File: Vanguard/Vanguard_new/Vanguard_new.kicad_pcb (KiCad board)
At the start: 4 copper layers, 683.3 x 251 mm, 70 parts, among them J1 USB_C, J2 Conn_02x03_Pin, J3 Micro_SD_Card_Det1, J4 STARBOARD_SERVO, J5 PORTSIDE_SERVO, Q1 BSS138, Q2 BSS138, Q3 BSS138, Q4 BSS138, U1 ATSAMD11D14A-M, U2 ATmega4809-A, U3 AT25DF641A-SH-T, U4 AP2112K-3.3, U5 MPM3610AGQV-P, U6 BNO086, U7 TXB0104D, U8 TPS61092, Y1 32.768kHz

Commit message: usb input almost done
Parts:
- added J6: LIPO_in, Wago-2601-1102:CONN2_2601-1102_WAG, F.Cu at (240.0, 114.5)
- J2: footprint Connector_PinHeader_2.54mm:PinHeader_1x03_P2.54mm_Vertical -> Connector_PinHeader_2.54mm:PinHeader_2x03_P2.54mm_Vertical
- moved Q3 311.1 mm to (354.8, 15.3), turned to -90 degrees
- moved Q2 310.5 mm to (352.8, 19.3)
- moved Q1 310.5 mm to (356.3, 19.3)
- moved U1 304.3 mm to (348.0, 16.3), turned to -45 degrees
- moved J1 303.2 mm to (336.8, 24.6), turned to 90 degrees
- moved J2 294.8 mm to (346.3, 27.9)
- moved D2 244.8 mm to (356.8, 25.4), turned to 0 degrees
- moved D3 244.7 mm to (355.0, 25.4), turned to 0 degrees
- moved TP1 236.5 mm to (342.3, 17.9), turned to 90 degrees
- moved D1 226.3 mm to (340.8, 24.4), turned to 180 degrees
- moved R7 225.3 mm to (357.3, 13.9), turned to 90 degrees
- moved TP2 223.8 mm to (338.3, 17.9), turned to 90 degrees
- moved R6 222.1 mm to (357.3, 22.4), turned to 90 degrees
- moved R12 221.5 mm to (357.3, 15.9)
- moved R5 221.1 mm to (358.3, 22.4)
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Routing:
- net RST: track 38.9 -> 84.4 mm, vias 0 -> 3
- net VBUS_out: track 15.0 -> 50.3 mm, vias 0 -> 4
- net UPDI: track 0.00 -> 28.0 mm, vias 0 -> 2
- net Net-(D1-I/O2): track 0.00 -> 26.5 mm, vias 0 -> 2
- net Net-(D1-I/O1): track 0.00 -> 20.3 mm, vias 0 -> 2
- net Net-(J2-Pin_2): track 0.00 -> 19.2 mm, vias 0 -> 2
- net Net-(D2-K): track 0.00 -> 17.9 mm, vias 0 -> 2
- net Net-(J2-Pin_6): track 0.00 -> 17.7 mm, vias 0 -> 2
- net /RX_UPDI: track 0.00 -> 17.6 mm
- net Net-(D3-K): track 0.00 -> 11.0 mm, vias 0 -> 2
- net GND: track 31.0 -> 37.9 mm
- net TX0: track 0.00 -> 6.48 mm, vias 0 -> 2
- net RX0: track 0.00 -> 2.51 mm
- net Net-(D2-A): track 0.00 -> 1.33 mm
- net Net-(D3-A): track 0.00 -> 1.00 mm

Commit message: pcb laying out
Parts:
- J6: value LIPO_in -> Conn_01x02_Pin; footprint Wago-2601-1102:CONN2_2601-1102_WAG -> Connector_PinHeader_2.54mm:PinHeader_1x02_P2.54mm_Vertical
- TP1, TP2: footprint TestPoint:TestPoint_2Pads_Pitch5.08mm_Drill1.3mm -> TestPoint:TestPoint_Pad_1.0x1.0mm
- moved U7 353.9 mm to (355.0, -11.9), turned to 0 degrees
- moved J3 332.3 mm to (343.1, -10.5), turned to 90 degrees
- moved U3 282.3 mm to (364.5, 18.0), turned to 180 degrees
- moved U2 224.7 mm to (357.7, 4.94), turned to 135 degrees
- moved R2 203.2 mm to (346.5, 25.0), turned to 90 degrees
- moved J6 169.3 mm to (378.5, 17.1)
- moved C10 157.8 mm to (374.1, 13.9), turned to 180 degrees
- moved C9 156.6 mm to (374.1, 14.7), turned to 180 degrees
- moved L1 154.0 mm to (370.9, 15.0), turned to 0 degrees
- moved U8 149.8 mm to (373.6, 18.4), turned to -90 degrees
- moved C8 146.5 mm to (369.8, 18.9), turned to 90 degrees
- moved TP2 1.70 mm to (340.0, 17.9)
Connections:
- J6 pad 1: GND -> VBUS_out
- J6 pad 2: unconnected-(J6-1_2-Pad2) -> GND
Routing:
- net RST: track 84.4 -> 123.4 mm, vias 3 -> 5
- net VBUS_out: track 50.3 -> 74.6 mm
- net PA3/SS: track 0.00 -> 19.2 mm, vias 0 -> 2
- net PA0/MISO: track 0.00 -> 18.5 mm, vias 0 -> 2
- net Net-(J2-Pin_3): track 0.00 -> 17.5 mm, vias 0 -> 2
- net D7: track 0.00 -> 16.1 mm, vias 0 -> 2
- net PA2/SCK: track 0.00 -> 15.8 mm, vias 0 -> 2
- net D4: track 0.00 -> 15.4 mm, vias 0 -> 2
- net D6: track 0.00 -> 15.0 mm
- net CD: track 0.00 -> 14.8 mm, vias 0 -> 2
- net D5: track 0.00 -> 14.1 mm, vias 0 -> 2
- net GND: track 37.9 -> 49.2 mm, vias 13 -> 15
- net PA1/MOSI: track 0.00 -> 10.9 mm
- net Net-(D1-I/O1): track 20.3 -> 30.1 mm
- net BUZZER: track 0.00 -> 9.17 mm
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
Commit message: finished pcb wiring
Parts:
- moved R21 296.2 mm to (359.5, 13.5)
- moved C2 294.3 mm to (337.0, 12.5), turned to 90 degrees
- moved ADR1 294.0 mm to (341.8, 8.06)
- moved C3 294.0 mm to (337.0, 14.2), turned to -90 degrees
- moved R18 293.9 mm to (346.4, 12.5)
- moved R19 293.9 mm to (346.4, 10.2)
- moved C7 293.9 mm to (346.0, 13.0)
- moved R20 293.9 mm to (344.8, 8.64)
- moved R23 293.9 mm to (344.6, 7.49)
- moved U6 293.9 mm to (343.1, 12.2)
- moved Y1 293.9 mm to (339.2, 12.3)
- moved R24 293.6 mm to (343.0, 16.0), turned to 0 degrees
- moved R22 292.8 mm to (361.5, 10.5), turned to 135 degrees
- moved R9 215.5 mm to (356.5, 12.0), turned to 180 degrees
- moved R10 213.4 mm to (354.2, 23.9), turned to 90 degrees
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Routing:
- net +5V: track 2.97 -> 78.5 mm, vias 0 -> 2
- net RST: track 123.4 -> 175.3 mm, vias 5 -> 12
- net GND: track 49.2 -> 81.2 mm, vias 15 -> 28
- net STAR_SERVO: track 0.00 -> 27.3 mm, vias 0 -> 1
- net PORT_SERVO: track 0.00 -> 27.2 mm, vias 0 -> 1
- net SCL: track 0.00 -> 25.2 mm, vias 0 -> 2
- net SDA: track 0.00 -> 23.8 mm, vias 0 -> 4
- net TX0: track 6.48 -> 19.0 mm, vias 2 -> 4
- net RX0: track 2.51 -> 14.5 mm, vias 0 -> 2
- net STAR_RED: track 0.00 -> 8.11 mm, vias 0 -> 2
- net UPDI: track 27.8 -> 35.4 mm, vias 2 -> 4
- net VBUS_out: track 74.6 -> 82.2 mm, vias 4 -> 6
- net PORT_RED: track 0.00 -> 7.05 mm
- net STAR_GREEN: track 0.00 -> 6.01 mm
- net PORT_GREEN: track 0.00 -> 5.59 mm, vias 0 -> 2
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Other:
- board size 683.3 x 251 mm -> 45 x 52.5 mm

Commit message: few silkscreen
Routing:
- net RST: track 175.3 -> 174.5 mm
- net Net-(J2-Pin_6): track 17.8 -> 18.4 mm

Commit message: small changes
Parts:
- moved Q4 257.4 mm to (134.0, 105.1)
- moved BZ1 256.0 mm to (144.6, 100.7)
- moved R11 252.6 mm to (121.0, 125.6), turned to 180 degrees
- moved C7 252.4 mm to (117.1, 119.4)
- moved C8 252.3 mm to (140.9, 124.9)
- moved STARBOARD_RGB1 252.3 mm to (141.0, 109.5)
- moved ADR1 252.3 mm to (112.9, 114.0)
- moved C1 252.3 mm to (115.5, 130.1)
- moved C10 252.3 mm to (145.1, 119.9)
- moved C4 252.3 mm to (132.5, 130.5)
- moved C5 252.3 mm to (142.5, 131.2)
- moved C6 252.3 mm to (146.2, 129.0)
- moved C9 252.3 mm to (145.1, 120.6)
- moved D1 252.3 mm to (111.8, 130.3)
- moved D2 252.3 mm to (127.8, 131.3)
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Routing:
- net +5V: track 78.5 -> 66.4 mm
- net BUZZER: track 9.17 -> 3.84 mm
- net Net-(U6-XIN32): track 5.51 -> 4.12 mm
- net Net-(BZ1--): track 7.23 -> 6.07 mm
- net Net-(U6-XOUT32/CLKSEL1): track 5.28 -> 4.19 mm
- net Net-(J2-Pin_6): track 18.4 -> 18.9 mm
- net GND: track 81.2 -> 80.8 mm, vias 28 -> 29
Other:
- board size 45 x 52.5 mm -> 46.2 x 50.9 mm

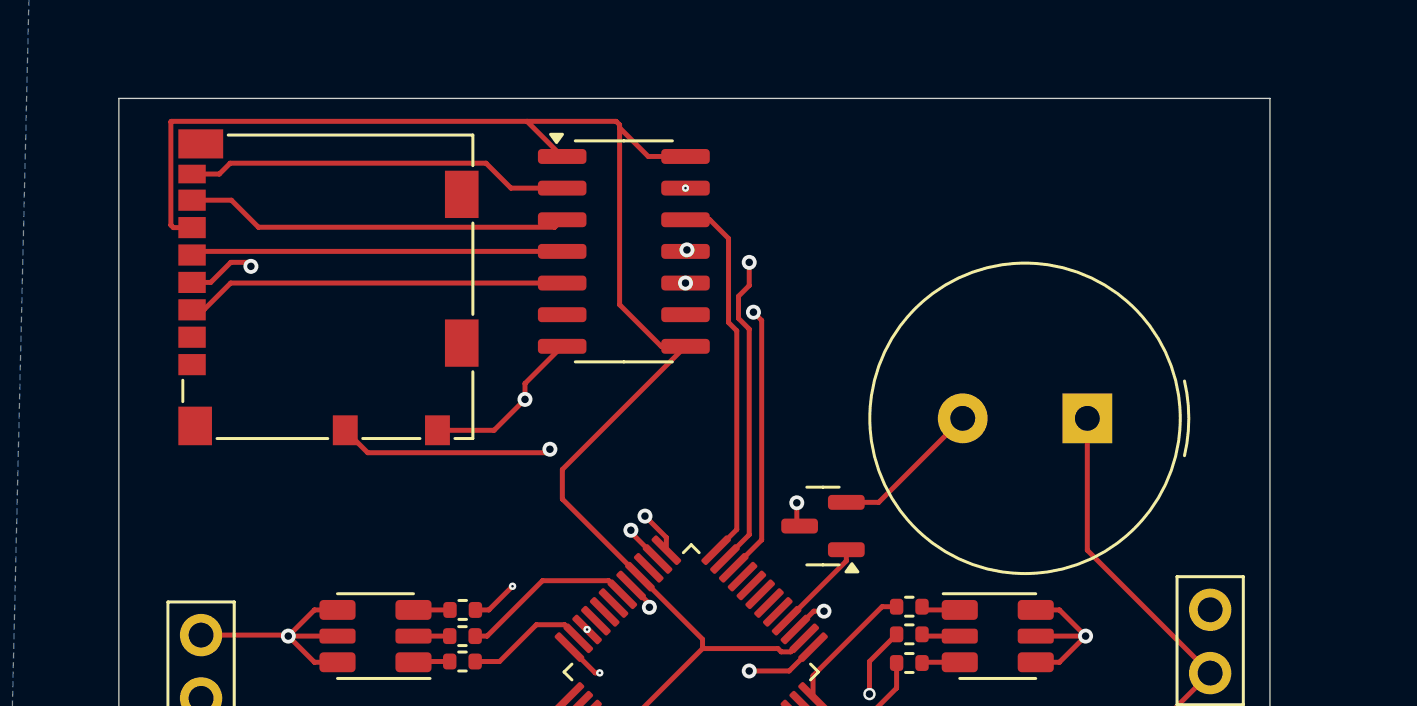
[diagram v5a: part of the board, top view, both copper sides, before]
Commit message: add 2 labels
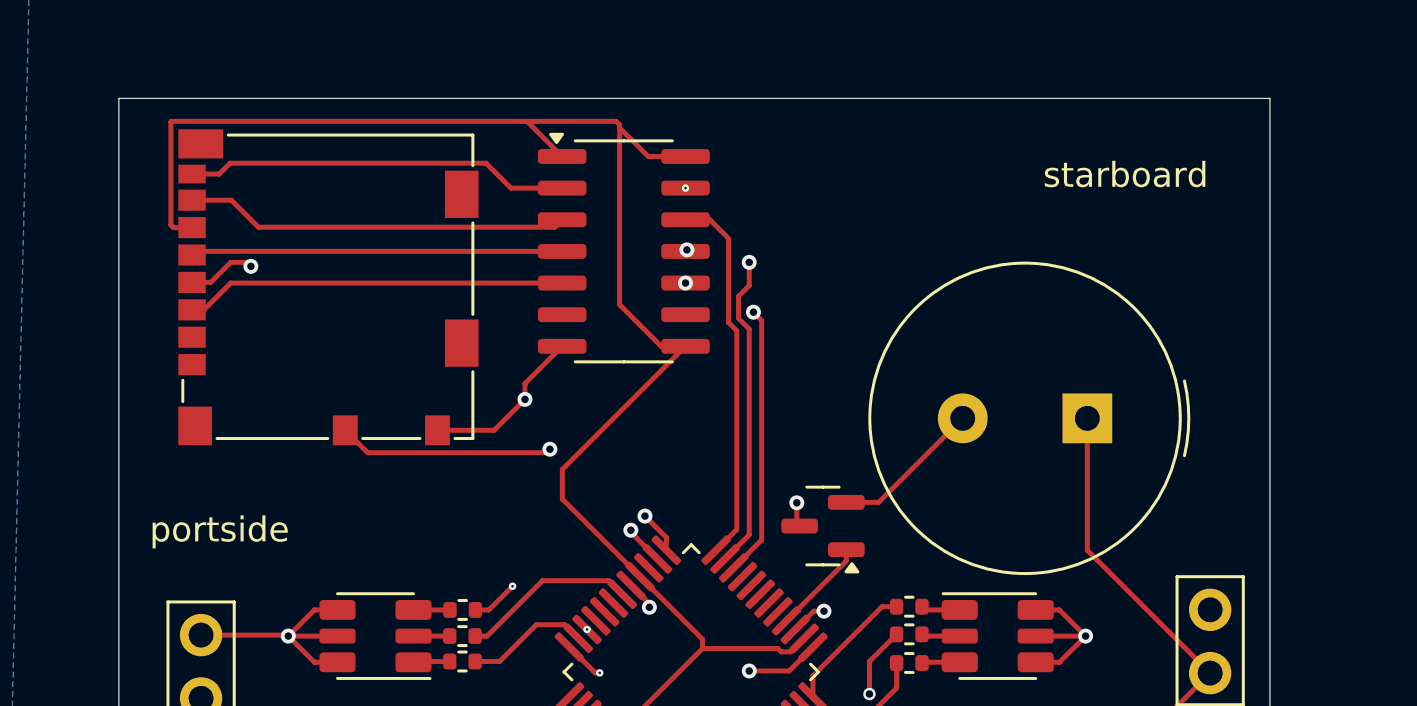
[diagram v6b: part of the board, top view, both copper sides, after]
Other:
- board text added: "portside"
- board text added: "starboard"
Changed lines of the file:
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@@
 		(tags "resistor")
 		(property "Reference" "R11"
-			(at 0 -1.17 360)
+			(at 0 -1.17 0)
 			(layer "F.SilkS")
 			(hide yes)
@@
 		)
 		(property "Value" "4k7"
-			(at 0 1.17 360)
+			(at 0 1.17 0)
 			(layer "F.Fab")
 			(effects
@@
 		)
 		(fp_text user "${REFERENCE}"
-			(at 0 0 360)
+			(at 0 0 0)
 			(layer "F.Fab")
 			(effects
@@
 		(tags "capacitor")
 		(property "Reference" "C2"
-			(at 28.55 -0.18 360)
+			(at 28.55 -0.18 0)
 			(layer "F.SilkS")
 			(hide yes)
@@
 		)
 		(property "Value" "22pF"
-			(at 28.550001 1.92 360)
+			(at 28.550001 1.92 0)
 			(layer "F.Fab")
 			(effects
@@
 		)
 		(fp_text user "${REFERENCE}"
-			(at 0 -0.680001 360)
+			(at 0 -0.680001 0)
 			(layer "F.Fab")
 			(effects
@@
 		(tags "capacitor")
 		(property "Reference" "C3"
-			(at 28.55 -0.18 360)
+			(at 28.55 -0.18 0)
 			(layer "F.SilkS")
 			(hide yes)
@@
 		)
 		(property "Value" "22pF"
-			(at 28.550001 1.92 360)
+			(at 28.550001 1.92 0)
 			(layer "F.Fab")
 			(effects
@@
 		)
 		(fp_text user "${REFERENCE}"
-			(at 0 -0.680001 360)
+			(at 0 -0.680001 0)
 			(layer "F.Fab")
 			(effects
@@
 		(layer "Edge.Cuts")
 	)
+	(gr_text "starboard"
+		(at 142.83 91.57 0)
+		(layer "F.SilkS")
+		(effects
+			(font
+				(size 1 1)
+				(thickness 0.1)
+			)
+			(justify left bottom)
+		)
+	)
+	(gr_text "portside"
+		(at 106.97 105.8 0)
+		(layer "F.SilkS")
+		(effects
+			(font
+				(size 1 1)
+				(thickness 0.1)
+			)
+			(justify left bottom)
+		)
+	)
 	(segment

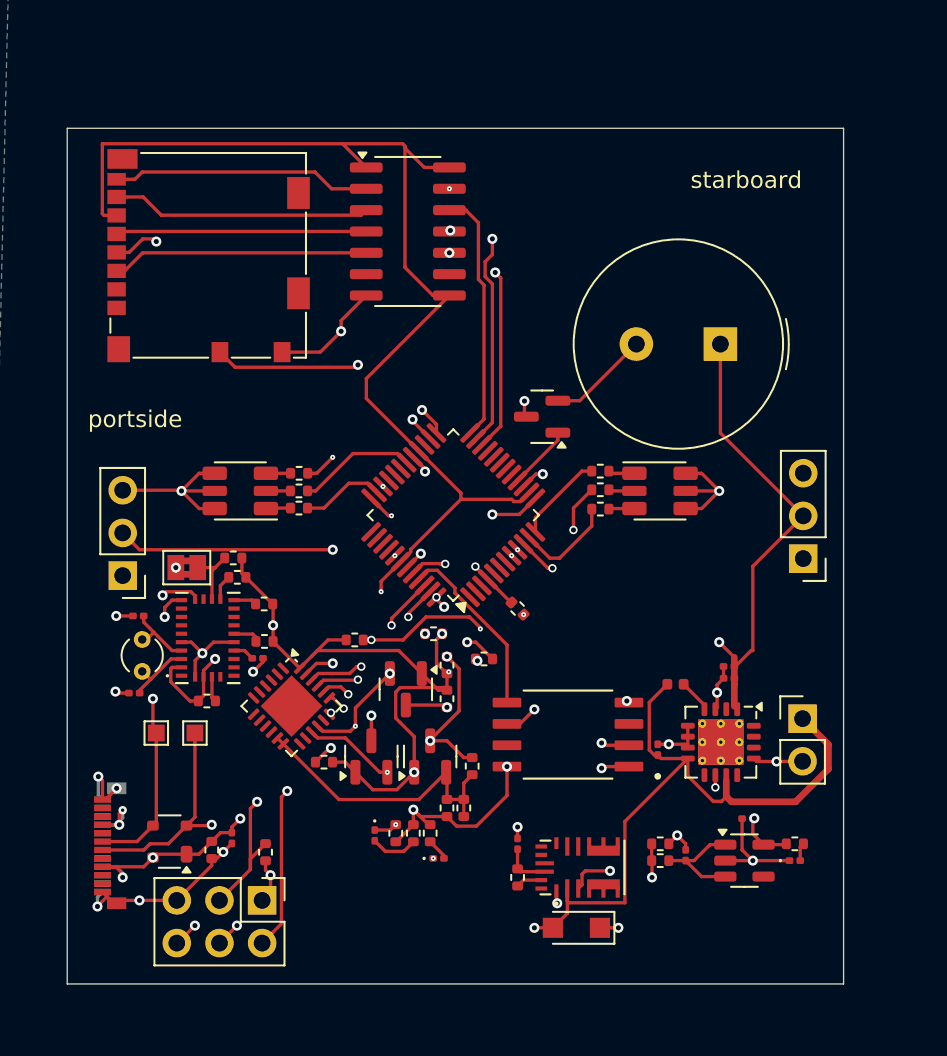
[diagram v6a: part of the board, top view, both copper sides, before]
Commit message: fixed sca pin and cleared some track-via clearnace issues
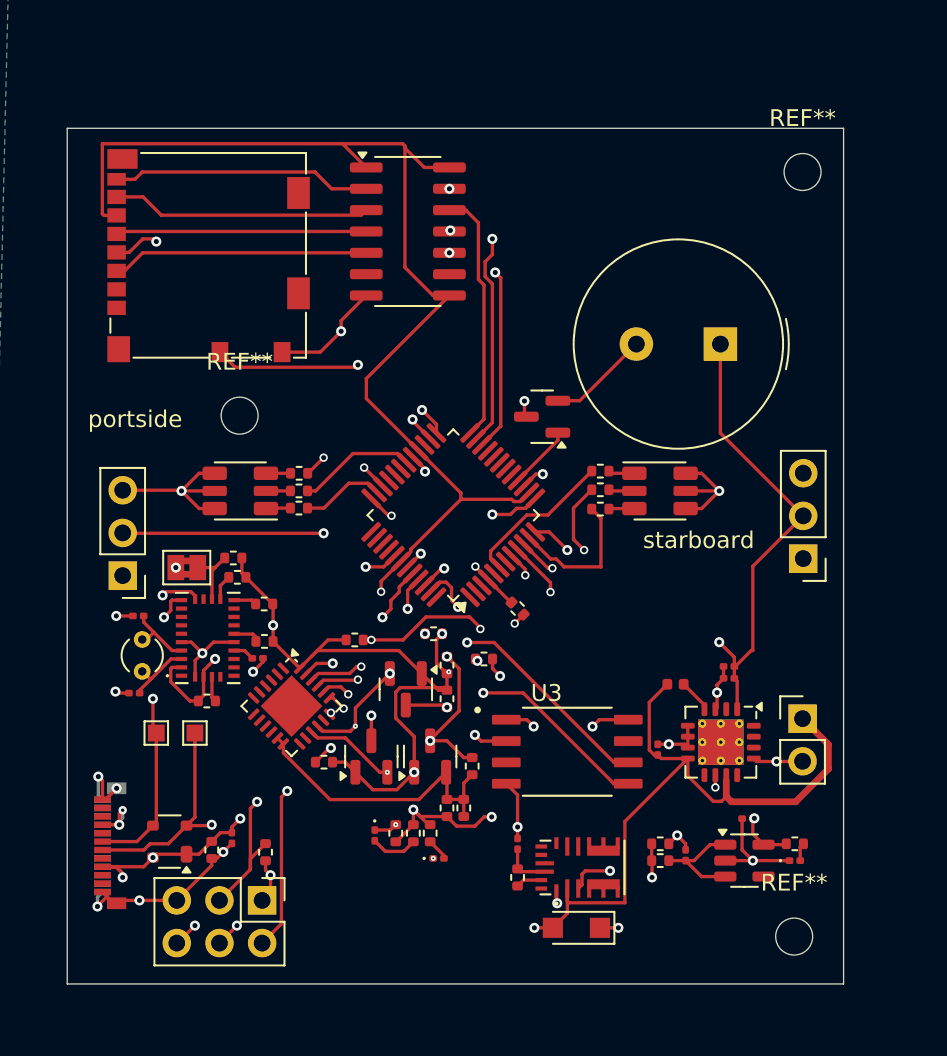
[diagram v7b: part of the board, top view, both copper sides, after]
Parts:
- added REF**: MountingHole_2.2mm_M2, MountingHole:MountingHole_2.2mm_M2, F.Cu at (149.0, 136.0)
- added REF**: MountingHole_2.2mm_M2, MountingHole:MountingHole_2.2mm_M2, F.Cu at (116.0, 105.0)
- added REF**: MountingHole_2.2mm_M2, MountingHole:MountingHole_2.2mm_M2, F.Cu at (149.5, 90.5)
- moved U3 1.02 mm to (135.5, 125.0), turned to 0 degrees
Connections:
- U2 pad 12: STAR_BLUE -> SDA
- U2 pad 48: SDA -> unconnected-(U2-PA4-Pad48)
- U2 pad 6: unconnected-(U2-PB2-Pad6) -> STAR_BLUE
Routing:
- net SDA: track 23.8 -> 40.7 mm, vias 4 -> 3
- net PA1/MOSI: track 10.9 -> 20.6 mm, vias 0 -> 2
- net RST: track 174.7 -> 179.4 mm, vias 12 -> 13
- net PA3/SS: track 19.2 -> 14.5 mm
- net STAR_BLUE: track 5.35 -> 9.20 mm
- net PA0/MISO: track 18.5 -> 14.7 mm
- net PA2/SCK: track 15.8 -> 19.1 mm
- net UPDI: track 35.4 -> 38.6 mm
- net STAR_GREEN: track 6.01 -> 8.63 mm
- net GND: track 80.8 -> 82.5 mm, vias 29 -> 28
- net STAR_RED: track 8.11 -> 9.54 mm
- net RX0: track 14.5 -> 15.2 mm
- net +5V: track 66.4 -> 65.7 mm
- net TX0: track 19.0 -> 19.7 mm

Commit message: schematic fixes
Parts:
- moved REF** 1.11 mm to (148.6, 91.2)
- moved R7 0.36 mm to (128.7, 119.8)
- moved REF** 0.27 mm to (148.9, 135.8)
- moved R28 0.21 mm to (119.6, 110.7)
- moved R30 0.17 mm to (119.6, 108.3)
- moved R16 0.15 mm to (141.0, 130.3)
- moved R4 0.12 mm to (127.3, 130.0)
- moved R5 0.12 mm to (129.5, 128.3)
- moved R29 0.07 mm to (119.6, 109.5)
- moved R6 0.05 mm to (128.4, 128.3)
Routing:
- net Net-(U5-FB): track 9.03 -> 1.15 mm, vias 2 -> 0
- net RST: track 179.4 -> 184.1 mm
- net Net-(D2-K): track 20.2 -> 22.2 mm
- net GND: track 82.5 -> 80.8 mm, vias 28 -> 27
- net Net-(J2-Pin_2): track 19.2 -> 20.8 mm
- net VBUS_out: track 81.7 -> 83.2 mm
- net Net-(D1-I/O1): track 30.1 -> 31.0 mm
- net STAR_GREEN: track 8.63 -> 7.85 mm
- net PORT_GREEN: track 5.58 -> 6.14 mm
